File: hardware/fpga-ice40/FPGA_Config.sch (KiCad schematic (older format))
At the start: 5 parts, among them U1 iCE40HX4K-TQ144, X1 ECS-2520MV-xxx-xx

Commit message: Reannotate schematic symbols
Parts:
- renumbered C43 to C44, R1 to R8, R2 to R9
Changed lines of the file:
@@
 P 3900 3600
 AR Path="/5F5C1BA6" Ref="R?"  Part="1"
-AR Path="/5F5B53E5/5F5C1BA6" Ref="R1"  Part="1"
-F 0 "R1" V 3950 3750 50  0000 L CNN
+AR Path="/5F5B53E5/5F5C1BA6" Ref="R8"  Part="1"
+F 0 "R8" V 3950 3750 50  0000 L CNN
 F 1 "10k" V 3950 3450 50  0000 R CNN
 F 2 "Resistor_SMD:R_0603_1608Metric" V 3830 3600 50  0001 C CNN
@@
 P 4000 3600
 AR Path="/5F5C1BB3" Ref="R?"  Part="1"
-AR Path="/5F5B53E5/5F5C1BB3" Ref="R2"  Part="1"
-F 0 "R2" V 4050 3750 50  0000 L CNN
+AR Path="/5F5B53E5/5F5C1BB3" Ref="R9"  Part="1"
+F 0 "R9" V 4050 3750 50  0000 L CNN
 F 1 "10k" V 4050 3450 50  0000 R CNN
 F 2 "Resistor_SMD:R_0603_1608Metric" V 3930 3600 50  0001 C CNN
@@
 P 7400 4650
 AR Path="/5F5C1BC2" Ref="#PWR?"  Part="1"
-AR Path="/5F5B53E5/5F5C1BC2" Ref="#PWR0133"  Part="1"
-F 0 "#PWR0133" H 7400 4400 50  0001 C CNN
+AR Path="/5F5B53E5/5F5C1BC2" Ref="#PWR032"  Part="1"
+F 0 "#PWR032" H 7400 4400 50  0001 C CNN
 F 1 "GND" H 7403 4524 50  0000 C CNN
 F 2 "" H 7300 4300 50  0001 C CNN
@@
 P 6700 4400
 AR Path="/5F5C1BD0" Ref="C?"  Part="1"
-AR Path="/5F5B53E5/5F5C1BD0" Ref="C43"  Part="1"
-F 0 "C43" H 6815 4446 50  0000 L CNN
+AR Path="/5F5B53E5/5F5C1BD0" Ref="C44"  Part="1"
+F 0 "C44" H 6815 4446 50  0000 L CNN
 F 1 "100n" H 6815 4355 50  0000 L CNN
 F 2 "Capacitor_SMD:C_0603_1608Metric" H 6738 4250 50  0001 C CNN
@@
 P 6700 4650
 AR Path="/5F5C1BD6" Ref="#PWR?"  Part="1"
-AR Path="/5F5B53E5/5F5C1BD6" Ref="#PWR0134"  Part="1"
-F 0 "#PWR0134" H 6700 4400 50  0001 C CNN
+AR Path="/5F5B53E5/5F5C1BD6" Ref="#PWR031"  Part="1"
+F 0 "#PWR031" H 6700 4400 50  0001 C CNN
 F 1 "GND" H 6703 4524 50  0000 C CNN
 F 2 "" H 6600 4300 50  0001 C CNN

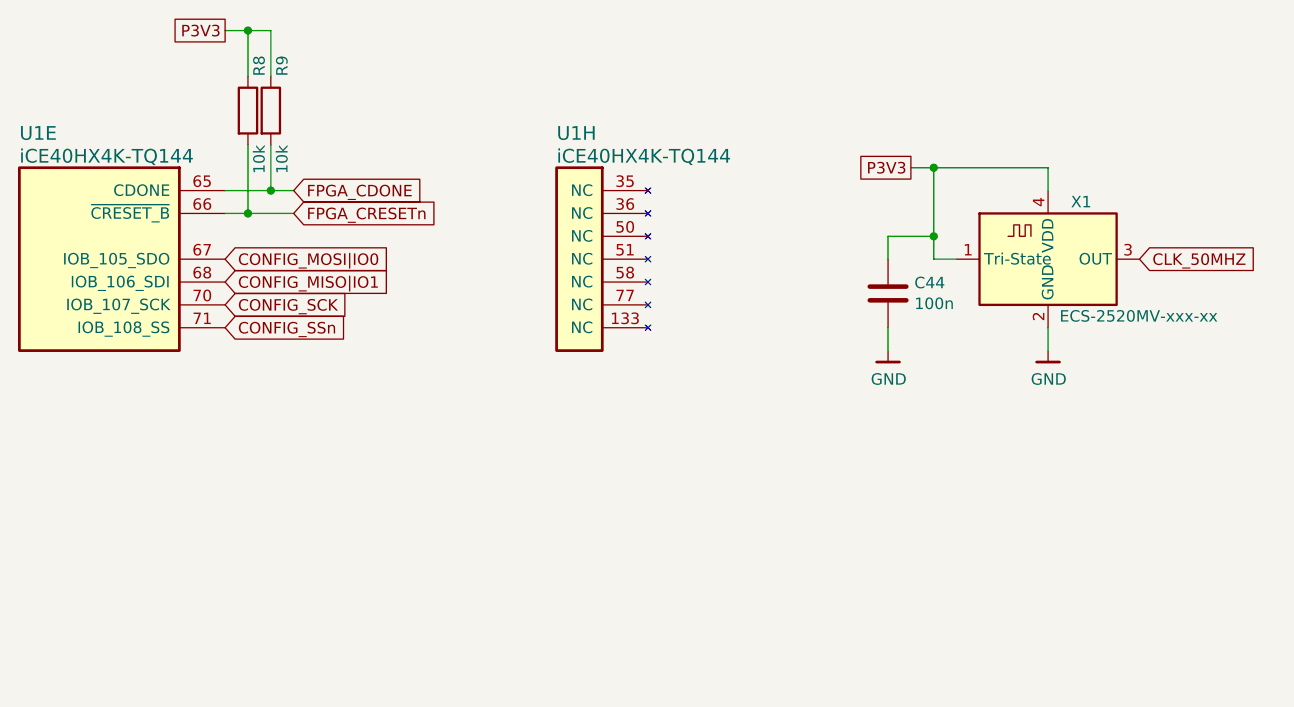
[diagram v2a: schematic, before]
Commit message: Flash programming header can hold FPGA in configuration reset
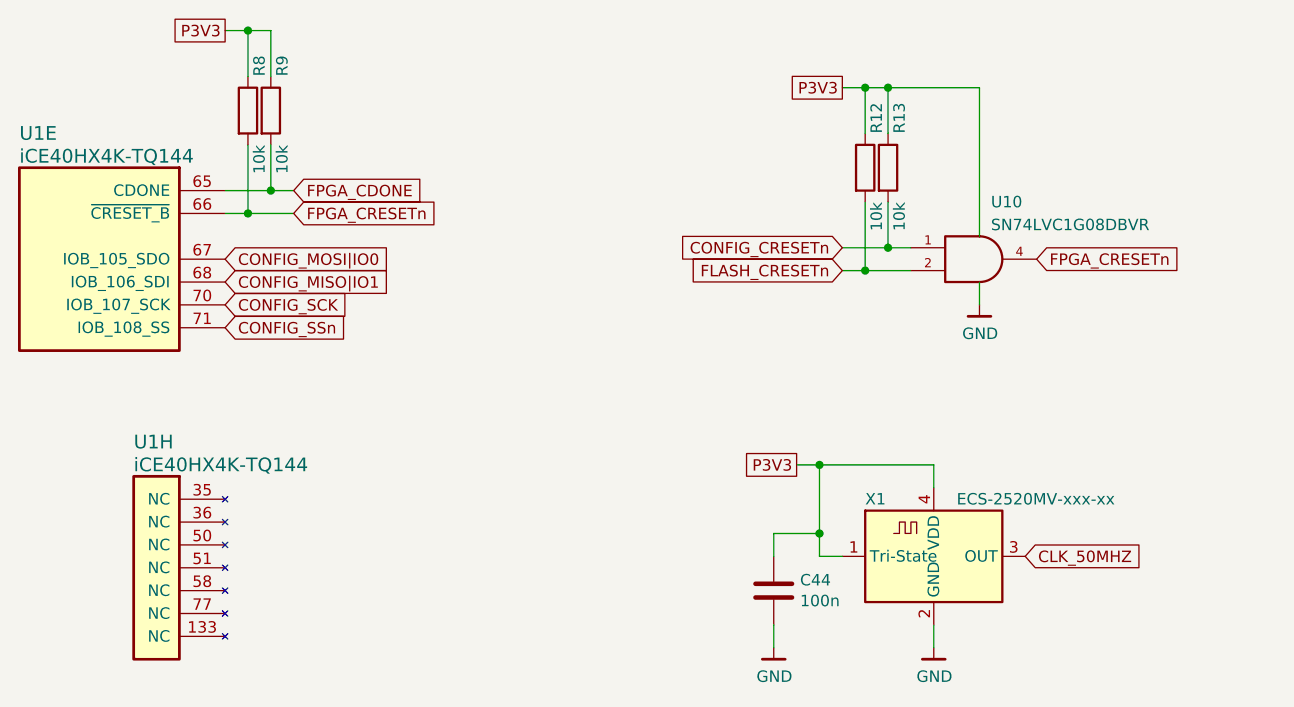
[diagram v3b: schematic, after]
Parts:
- added R12, R13: 10k, Resistor_SMD:R_0603_1608Metric, symbol Device:R
- added U10: SN74LVC1G08DBVR, Package_TO_SOT_SMD:SOT-23-5, symbol 74xGxx:74AHC1G08
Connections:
- net FPGA_CRESETn: now also U10.4
- net GND: now also U10.3 (GND)
- net P3V3 renamed VCC
- net VCC: now also R12.1, R13.1, U10.5 (VCC)
- new net CONFIG_CRESETn: R13.2, U10.1
- new net FLASH_CRESETn: R12.2, U10.2
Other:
- moved on the sheet: C44, U1H, X1
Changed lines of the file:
@@
 $Descr USLetter 11000 8500
 encoding utf-8
-Sheet 4 12
+Sheet 11 12
 Title "Ferk-Cart iCE40 Devboard"
 Date "2020-06-29"
@@
 L ng_fpga_lattice_ice40:iCE40HX4K-TQ144 U?
 U 8 1 5F5C1B96
-P 5650 3950
+P 3800 5300
 AR Path="/5F5C1B96" Ref="U?"  Part="8"
 AR Path="/5F5B53E5/5F5C1B96" Ref="U1"  Part="8"
-F 0 "U1" H 6050 4200 60  0000 R CNN
-F 1 "iCE40HX4K-TQ144" H 6050 4100 60  0000 R CNN
-F 2 "Package_QFP:TQFP-144_20x20mm_P0.5mm" H 5850 4000 60  0001 L CNN
-F 3 "https://www.mouser.com/datasheet/2/225/FPGA-DS-02029-3-5-iCE40-LP-HX-Family-Data-Sheet-1022803.pdf" H 5850 3800 60  0001 L CNN
-F 4 "iCE40HX4K-TQ144" H 5850 3900 60  0001 L CNN "manf#"
-	8    5650 3950
+F 0 "U1" H 4200 5550 60  0000 R CNN
+F 1 "iCE40HX4K-TQ144" H 4200 5450 60  0000 R CNN
+F 2 "Package_QFP:TQFP-144_20x20mm_P0.5mm" H 4000 5350 60  0001 L CNN
+F 3 "https://www.mouser.com/datasheet/2/225/FPGA-DS-02029-3-5-iCE40-LP-HX-Family-Data-Sheet-1022803.pdf" H 4000 5150 60  0001 L CNN
+F 4 "iCE40HX4K-TQ144" H 4000 5250 60  0001 L CNN "manf#"
+	8    3800 5300
 	-1   0    0    -1
 $EndComp
@@
 L Oscillator:ECS-2520MV-xxx-xx X?
 U 1 1 5F5C1BBC
-P 7400 4250
+P 6900 5550
 AR Path="/5F5C1BBC" Ref="X?"  Part="1"
 AR Path="/5F5B53E5/5F5C1BBC" Ref="X1"  Part="1"
-F 0 "X1" H 7500 4500 50  0000 L CNN
-F 1 "ECS-2520MV-xxx-xx" H 7450 4000 50  0000 L CNN
-F 2 "ng_time:Oscillator_2.5x2.0" H 7850 3900 50  0001 C CNN
-F 3 "https://www.ecsxtal.com/store/pdf/ECS-2520MV.pdf" H 7225 4375 50  0001 C CNN
-	1    7400 4250
+F 0 "X1" H 6600 5800 50  0000 L CNN
+F 1 "ECS-2520MV-xxx-xx" H 7000 5800 50  0000 L CNN
+F 2 "ng_time:Oscillator_2.5x2.0" H 7350 5200 50  0001 C CNN
+F 3 "https://www.ecsxtal.com/store/pdf/ECS-2520MV.pdf" H 6725 5675 50  0001 C CNN
+	1    6900 5550
 	1    0    0    -1
 $EndComp
@@
 L ng_power:GND #PWR?
 U 1 1 5F5C1BC2
-P 7400 4650
+P 6900 5950
 AR Path="/5F5C1BC2" Ref="#PWR?"  Part="1"
 AR Path="/5F5B53E5/5F5C1BC2" Ref="#PWR032"  Part="1"
-F 0 "#PWR032" H 7400 4400 50  0001 C CNN
-F 1 "GND" H 7403 4524 50  0000 C CNN
-F 2 "" H 7300 4300 50  0001 C CNN
-F 3 "" H 7400 4650 50  0001 C CNN
-	1    7400 4650
-	1    0    0    -1
-$EndComp
-Text GLabel 6800 3850 0    50   UnSpc ~ 0
+F 0 "#PWR032" H 6900 5700 50  0001 C CNN
+F 1 "GND" H 6903 5824 50  0000 C CNN
+F 2 "" H 6800 5600 50  0001 C CNN
+F 3 "" H 6900 5950 50  0001 C CNN
+	1    6900 5950
+	1    0    0    -1
+$EndComp
+Text GLabel 6300 5150 0    50   UnSpc ~ 0
 P3V3
 Wire Wire Line
-	7000 4250 6900 4250
-Wire Wire Line
-	6900 4250 6900 4150
-Wire Wire Line
-	6900 3850 7400 3850
-Wire Wire Line
-	7400 3850 7400 3950
-Wire Wire Line
-	6800 3850 6900 3850
-Wire Wire Line
-	7400 4650 7400 4550
-Text GLabel 7800 4250 2    50   Input ~ 0
+	6500 5550 6400 5550
+Wire Wire Line
+	6400 5550 6400 5450
+Wire Wire Line
+	6400 5150 6900 5150
+Wire Wire Line
+	6900 5150 6900 5250
+Wire Wire Line
+	6300 5150 6400 5150
+Wire Wire Line
+	6900 5950 6900 5850
+Text GLabel 7300 5550 2    50   Input ~ 0
 CLK_50MHZ
 $Comp
 L Device:C C?
 U 1 1 5F5C1BD0
-P 6700 4400
+P 6200 5700
 AR Path="/5F5C1BD0" Ref="C?"  Part="1"
 AR Path="/5F5B53E5/5F5C1BD0" Ref="C44"  Part="1"
-F 0 "C44" H 6815 4446 50  0000 L CNN
-F 1 "100n" H 6815 4355 50  0000 L CNN
-F 2 "Capacitor_SMD:C_0603_1608Metric" H 6738 4250 50  0001 C CNN
-F 3 "~" H 6700 4400 50  0001 C CNN
-	1    6700 4400
+F 0 "C44" H 6315 5746 50  0000 L CNN
+F 1 "100n" H 6315 5655 50  0000 L CNN
+F 2 "Capacitor_SMD:C_0603_1608Metric" H 6238 5550 50  0001 C CNN
+F 3 "~" H 6200 5700 50  0001 C CNN
+	1    6200 5700
 	1    0    0    -1
 $EndComp
@@
 L ng_power:GND #PWR?
 U 1 1 5F5C1BD6
-P 6700 4650
+P 6200 5950
 AR Path="/5F5C1BD6" Ref="#PWR?"  Part="1"
 AR Path="/5F5B53E5/5F5C1BD6" Ref="#PWR031"  Part="1"
-F 0 "#PWR031" H 6700 4400 50  0001 C CNN
-F 1 "GND" H 6703 4524 50  0000 C CNN
-F 2 "" H 6600 4300 50  0001 C CNN
-F 3 "" H 6700 4650 50  0001 C CNN
-	1    6700 4650
-	1    0    0    -1
-$EndComp
-Wire Wire Line
-	6700 4650 6700 4550
-Wire Wire Line
-	6700 4250 6700 4150
-Wire Wire Line
-	6700 4150 6900 4150
-Connection ~ 6900 4150
-Wire Wire Line
-	6900 4150 6900 3850
-Connection ~ 6900 3850
+F 0 "#PWR031" H 6200 5700 50  0001 C CNN
+F 1 "GND" H 6203 5824 50  0000 C CNN
+F 2 "" H 6100 5600 50  0001 C CNN
+F 3 "" H 6200 5950 50  0001 C CNN
+	1    6200 5950
+	1    0    0    -1
+$EndComp
+Wire Wire Line
+	6200 5950 6200 5850
+Wire Wire Line
+	6200 5550 6200 5450
+Wire Wire Line
+	6200 5450 6400 5450
+Connection ~ 6400 5450
+Wire Wire Line
+	6400 5450 6400 5150
+Connection ~ 6400 5150
+$Comp
+L 74xGxx:74AHC1G08 U10
+U 1 1 5EFB1490
+P 7100 4250
+F 0 "U10" H 7150 4500 50  0000 L CNN
+F 1 "SN74LVC1G08DBVR" H 7150 4400 50  0000 L CNN
+F 2 "Package_TO_SOT_SMD:SOT-23-5" H 7100 4250 50  0001 C CNN
+F 3 "http://www.ti.com/lit/sg/scyt129e/scyt129e.pdf" H 7100 4250 50  0001 C CNN
+	1    7100 4250
+	1    0    0    -1
+$EndComp
+Wire Wire Line
+	7100 4350 7100 4450
+Wire Wire Line
+	7100 4150 7100 3500
+Wire Wire Line
+	7100 3500 6700 3500
+$Comp
+L ng_power:GND #PWR035
+U 1 1 5EFB47F2
+P 7100 4450
+F 0 "#PWR035" H 7100 4200 50  0001 C CNN
+F 1 "GND" H 7103 4324 50  0000 C CNN
+F 2 "" H 7000 4100 50  0001 C CNN
+F 3 "" H 7100 4450 50  0001 C CNN
+	1    7100 4450
+	1    0    0    -1
+$EndComp
+Text GLabel 7350 4250 2    50   Input ~ 0
+FPGA_CRESETn
+Wire Wire Line
+	6600 4000 6600 4300
+$Comp
+L Device:R R?
+U 1 1 5EFB670F
+P 6600 3850
+AR Path="/5EFB670F" Ref="R?"  Part="1"
+AR Path="/5F5B53E5/5EFB670F" Ref="R12"  Part="1"
+F 0 "R12" V 6650 4000 50  0000 L CNN
+F 1 "10k" V 6650 3700 50  0000 R CNN
+F 2 "Resistor_SMD:R_0603_1608Metric" V 6530 3850 50  0001 C CNN
+F 3 "~" H 6600 3850 50  0001 C CNN
+	1    6600 3850
+	1    0    0    -1
+$EndComp
+Wire Wire Line
+	6700 4200 6700 4000
+Wire Wire Line
+	6600 3700 6600 3500
+Wire Wire Line
+	6600 3500 6700 3500
+Wire Wire Line
+	6700 3500 6700 3700
+$Comp
+L Device:R R?
+U 1 1 5EFB671D
+P 6700 3850
+AR Path="/5EFB671D" Ref="R?"  Part="1"
+AR Path="/5F5B53E5/5EFB671D" Ref="R13"  Part="1"
+F 0 "R13" V 6750 4000 50  0000 L CNN
+F 1 "10k" V 6750 3700 50  0000 R CNN
+F 2 "Resistor_SMD:R_0603_1608Metric" V 6630 3850 50  0001 C CNN
+F 3 "~" H 6700 3850 50  0001 C CNN
+	1    6700 3850
+	1    0    0    -1
+$EndComp
+Text GLabel 6500 3500 0    50   UnSpc ~ 0
+P3V3
+Wire Wire Line
+	6500 3500 6600 3500
+Connection ~ 6600 3500
+Connection ~ 6700 3500
+Wire Wire Line
+	6800 4200 6700 4200
+Connection ~ 6700 4200
+Wire Wire Line
+	6700 4200 6500 4200
+Wire Wire Line
+	6800 4300 6600 4300
+Connection ~ 6600 4300
+Wire Wire Line
+	6600 4300 6500 4300
+Text GLabel 6500 4300 0    50   Input ~ 0
+FLASH_CRESETn
+Text GLabel 6500 4200 0    50   Input ~ 0
+CONFIG_CRESETn
 $EndSCHEMATC
